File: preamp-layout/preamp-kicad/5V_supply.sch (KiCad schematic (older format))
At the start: 20 parts, among them J12 Conn_01x02_Male, J13 Conn_01x02_Male, J14 Conn_01x02_Male, J15 Screw_Terminal_01x03, T2 Transformer_1P_2S, U3 L7805

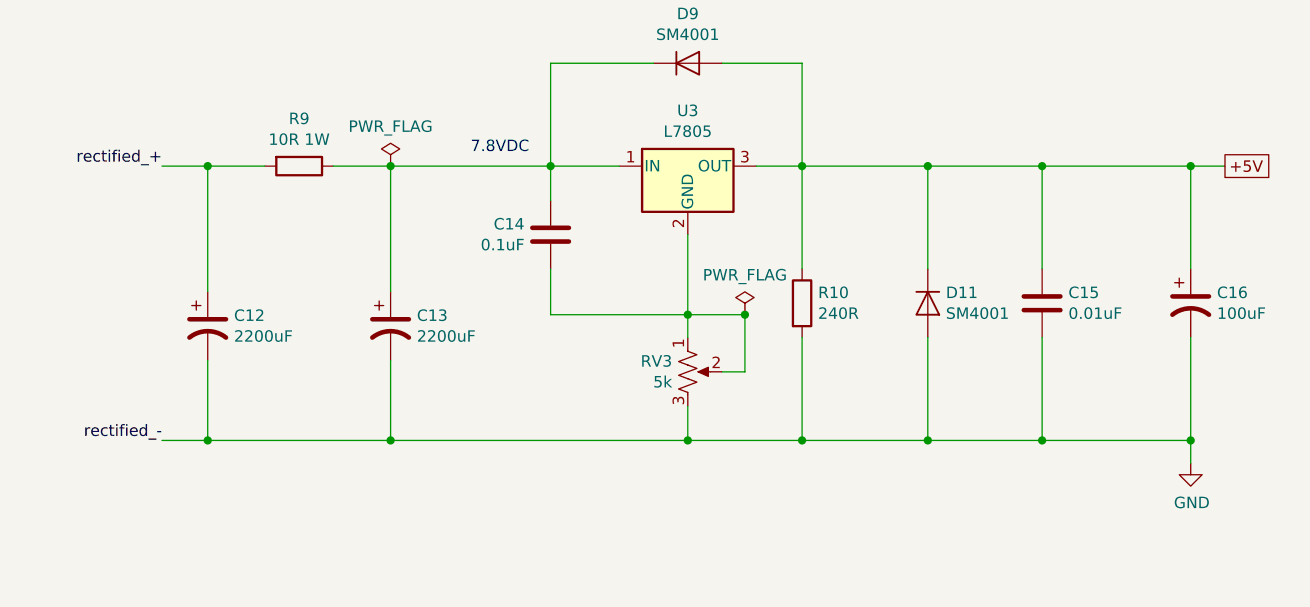
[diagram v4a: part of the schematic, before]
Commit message: Footprint assignment updates
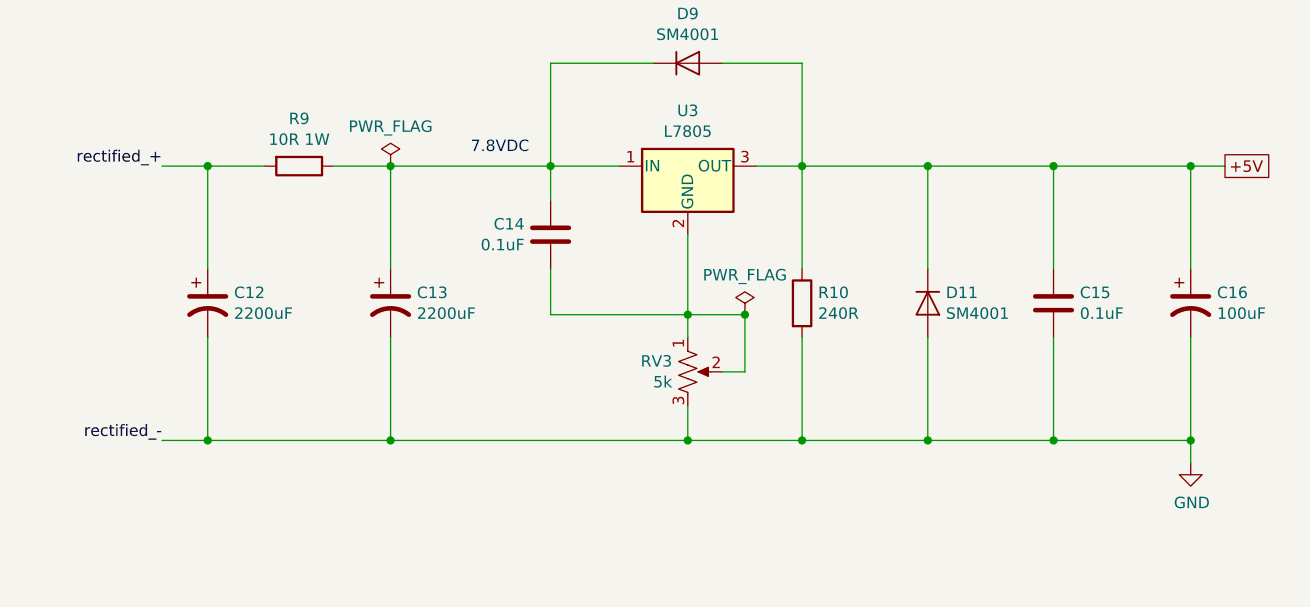
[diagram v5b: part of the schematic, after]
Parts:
- C12, C13: footprint (none) -> Capacitor_THT:CP_Radial_D12.5mm_P5.00mm
- C14: footprint (none) -> Capacitor_SMD:C_0805_2012Metric_Pad1.15x1.40mm_HandSolder
- C15: value 0.01uF -> 0.1uF; footprint (none) -> Capacitor_SMD:C_0805_2012Metric_Pad1.15x1.40mm_HandSolder
- C16: footprint (none) -> Capacitor_THT:CP_Radial_D6.3mm_P2.50mm
- R10: footprint (none) -> Resistor_SMD:R_1206_3216Metric_Pad1.42x1.75mm_HandSolder
- R9: footprint (none) -> Resistor_THT:R_Axial_DIN0414_L11.9mm_D4.5mm_P15.24mm_Horizontal
- U3: footprint (none) -> Package_TO_SOT_THT:TO-220-3_Vertical
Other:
- moved on the sheet: C12, C13, C15
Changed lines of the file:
@@
 L Device:C C?
 U 1 1 5FCCFC4E
-P 7500 4400
+P 7550 4400
 AR Path="/5FCCFC4E" Ref="C?"  Part="1"
 AR Path="/5E27B612/5FCCFC4E" Ref="C?"  Part="1"
 AR Path="/5E5EF2D4/5FCCFC4E" Ref="C15"  Part="1"
-F 0 "C15" H 7615 4446 50  0000 L CNN
-F 1 "0.01uF" H 7615 4355 50  0000 L CNN
-F 2 "" H 7538 4250 50  0001 C CNN
-F 3 "~" H 7500 4400 50  0001 C CNN
-	1    7500 4400
+F 0 "C15" H 7665 4446 50  0000 L CNN
+F 1 "0.1uF" H 7665 4355 50  0000 L CNN
+F 2 "Capacitor_SMD:C_0805_2012Metric_Pad1.15x1.40mm_HandSolder" H 7588 4250 50  0001 C CNN
+F 3 "~" H 7550 4400 50  0001 C CNN
+	1    7550 4400
 	1    0    0    -1
 $EndComp
@@
 F 0 "R10" H 6520 4446 50  0000 L CNN
 F 1 "240R" H 6520 4355 50  0000 L CNN
-F 2 "" V 6380 4400 50  0001 C CNN
+F 2 "Resistor_SMD:R_1206_3216Metric_Pad1.42x1.75mm_HandSolder" V 6380 4400 50  0001 C CNN
 F 3 "~" H 6450 4400 50  0001 C CNN
 	1    6450 4400
@@
 F 0 "R9" V 4043 3800 50  0000 C CNN
 F 1 "10R 1W" V 4134 3800 50  0000 C CNN
-F 2 "" V 4180 3800 50  0001 C CNN
+F 2 "Resistor_THT:R_Axial_DIN0414_L11.9mm_D4.5mm_P15.24mm_Horizontal" V 4180 3800 50  0001 C CNN
 F 3 "~" H 4250 3800 50  0001 C CNN
 	1    4250 3800
@@
 Connection ~ 5350 3800
 Wire Wire Line
-	3850 3800 4100 3800
-Wire Wire Line
 	5950 4850 5950 5000
-Connection ~ 4650 5000
 Connection ~ 5950 5000
 $Comp
@@
 F 0 "C14" H 5236 4146 50  0000 R CNN
 F 1 "0.1uF" H 5236 4055 50  0000 R CNN
-F 2 "" H 5388 3950 50  0001 C CNN
+F 2 "Capacitor_SMD:C_0805_2012Metric_Pad1.15x1.40mm_HandSolder" H 5388 3950 50  0001 C CNN
 F 3 "~" H 5350 4100 50  0001 C CNN
 	1    5350 4100
 	1    0    0    -1
 $EndComp
-$Comp
-L Device:CP1 C?
-U 1 1 5FCCFCBE
-P 3850 4500
-AR Path="/5FCCFCBE" Ref="C?"  Part="1"
-AR Path="/5E27B612/5FCCFCBE" Ref="C?"  Part="1"
-AR Path="/5E5EF2D4/5FCCFCBE" Ref="C12"  Part="1"
-F 0 "C12" H 3965 4546 50  0000 L CNN
-F 1 "2200uF" H 3965 4455 50  0000 L CNN
-F 2 "" H 3850 4500 50  0001 C CNN
-F 3 "~" H 3850 4500 50  0001 C CNN
-	1    3850 4500
-	1    0    0    -1
-$EndComp
-$Comp
-L Device:CP1 C?
-U 1 1 5FCCFCC4
-P 4650 4500
-AR Path="/5FCCFCC4" Ref="C?"  Part="1"
-AR Path="/5E27B612/5FCCFCC4" Ref="C?"  Part="1"
-AR Path="/5E5EF2D4/5FCCFCC4" Ref="C13"  Part="1"
-F 0 "C13" H 4765 4546 50  0000 L CNN
-F 1 "2200uF" H 4765 4455 50  0000 L CNN
-F 2 "" H 4650 4500 50  0001 C CNN
-F 3 "~" H 4650 4500 50  0001 C CNN
-	1    4650 4500
-	1    0    0    -1
-$EndComp
 Wire Wire Line
 	6100 3350 6450 3350
@@
 Wire Wire Line
 	5350 3350 5350 3800
-Wire Wire Line
-	3850 5000 4650 5000
-Wire Wire Line
-	3850 4350 3850 3800
-Wire Wire Line
-	4650 4350 4650 3800
-Wire Wire Line
-	3850 4650 3850 5000
-Wire Wire Line
-	4650 4650 4650 5000
 Wire Wire Line
 	4650 3800 5350 3800
 Connection ~ 4650 3800
 Wire Wire Line
-	7500 4250 7500 3800
-Connection ~ 7500 3800
+	7550 4250 7550 3800
 Wire Wire Line
 	8150 4250 8150 3800
@@
 F 0 "C16" H 8265 4446 50  0000 L CNN
 F 1 "100uF" H 8265 4355 50  0000 L CNN
-F 2 "" H 8150 4400 50  0001 C CNN
+F 2 "Capacitor_THT:CP_Radial_D6.3mm_P2.50mm" H 8150 4400 50  0001 C CNN
 F 3 "~" H 8150 4400 50  0001 C CNN
 	1    8150 4400
@@
 F 0 "U3" H 5950 4042 50  0000 C CNN
 F 1 "L7805" H 5950 3951 50  0000 C CNN
-F 2 "" H 5975 3650 50  0001 L CIN
+F 2 "Package_TO_SOT_THT:TO-220-3_Vertical" H 5975 3650 50  0001 L CIN
 F 3 "http://www.st.com/content/ccc/resource/technical/document/datasheet/41/4f/b3/b0/12/d4/47/88/CD00000444.pdf/files/CD00000444.pdf/jcr:content/translations/en.CD00000444.pdf" H 5950 3750 50  0001 C CNN
 	1    5950 3800
@@
 	6200 4450 5950 4450
 Wire Wire Line
-	4650 5000 5950 5000
-Wire Wire Line
 	5350 3800 5350 3950
 Wire Wire Line
@@
 Connection ~ 7000 5000
 Wire Wire Line
-	7000 5000 7500 5000
-Wire Wire Line
-	7500 4550 7500 5000
-Connection ~ 7500 5000
-Wire Wire Line
-	7500 5000 8150 5000
-Wire Wire Line
-	7500 3800 8150 3800
-Wire Wire Line
-	7000 3800 7500 3800
+	7550 4550 7550 5000
 Wire Wire Line
 	8150 5100 8150 5000
 Connection ~ 8150 5000
-Wire Wire Line
-	3850 3800 3650 3800
-Connection ~ 3850 3800
-Wire Wire Line
-	3850 5000 3650 5000
-Connection ~ 3850 5000
 Wire Wire Line
 	1550 5850 1550 5950
@@
 Wire Wire Line
 	4400 1500 4400 1700
+$Comp
+L Device:CP1 C?
+U 1 1 5FCCFCC4
+P 4650 4400
+AR Path="/5FCCFCC4" Ref="C?"  Part="1"
+AR Path="/5E27B612/5FCCFCC4" Ref="C?"  Part="1"
+AR Path="/5E5EF2D4/5FCCFCC4" Ref="C13"  Part="1"
+F 0 "C13" H 4765 4446 50  0000 L CNN
+F 1 "2200uF" H 4765 4355 50  0000 L CNN
+F 2 "Capacitor_THT:CP_Radial_D12.5mm_P5.00mm" H 4650 4400 50  0001 C CNN
+F 3 "~" H 4650 4400 50  0001 C CNN
+	1    4650 4400
+	1    0    0    -1
+$EndComp
+$Comp
+L Device:CP1 C?
+U 1 1 5FCCFCBE
+P 3850 4400
+AR Path="/5FCCFCBE" Ref="C?"  Part="1"
+AR Path="/5E27B612/5FCCFCBE" Ref="C?"  Part="1"
+AR Path="/5E5EF2D4/5FCCFCBE" Ref="C12"  Part="1"
+F 0 "C12" H 3965 4446 50  0000 L CNN
+F 1 "2200uF" H 3965 4355 50  0000 L CNN
+F 2 "Capacitor_THT:CP_Radial_D12.5mm_P5.00mm" H 3850 4400 50  0001 C CNN
+F 3 "~" H 3850 4400 50  0001 C CNN
+	1    3850 4400
+	1    0    0    -1
+$EndComp
+Wire Wire Line
+	3650 3800 3850 3800
+Wire Wire Line
+	3650 5000 3850 5000
+Wire Wire Line
+	3850 4250 3850 3800
+Connection ~ 3850 3800
+Wire Wire Line
+	3850 3800 4100 3800
+Wire Wire Line
+	4650 4250 4650 3800
+Wire Wire Line
+	3850 4550 3850 5000
+Connection ~ 3850 5000
+Wire Wire Line
+	3850 5000 4650 5000
+Wire Wire Line
+	4650 4550 4650 5000
+Connection ~ 4650 5000
+Wire Wire Line
+	4650 5000 5950 5000
+Connection ~ 7550 3800
+Wire Wire Line
+	7550 3800 8150 3800
+Connection ~ 7550 5000
+Wire Wire Line
+	7550 5000 8150 5000
+Wire Wire Line
+	7000 5000 7550 5000
+Wire Wire Line
+	7000 3800 7550 3800
 $EndSCHEMATC

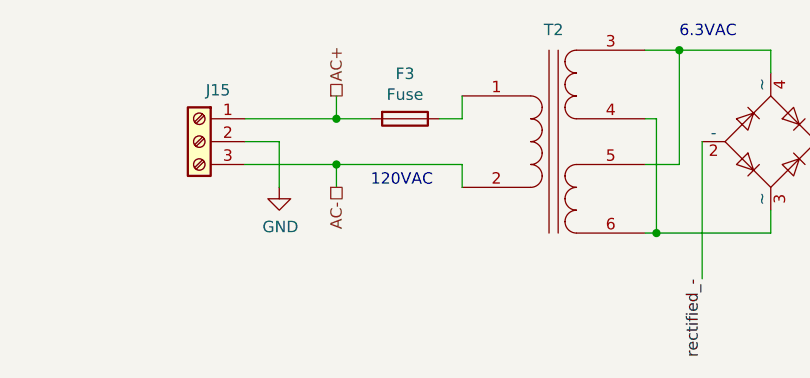
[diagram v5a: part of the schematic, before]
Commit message: Footprint updates
Footprint creation of relay, ESP32
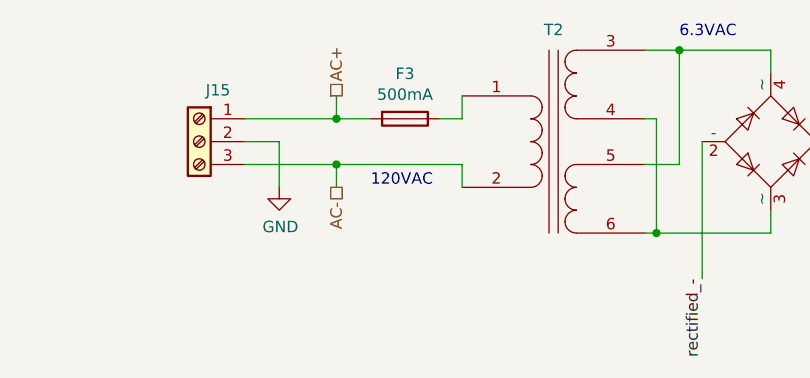
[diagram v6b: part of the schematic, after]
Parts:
- D11, D9: footprint (none) -> Diode_SMD:D_SOD-123F
- F3: value Fuse -> 500mA
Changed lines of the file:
@@
 F 0 "D9" H 5950 3566 50  0000 C CNN
 F 1 "SM4001" H 5950 3475 50  0000 C CNN
-F 2 "" H 5950 3350 50  0001 C CNN
+F 2 "Diode_SMD:D_SOD-123F" H 5950 3350 50  0001 C CNN
 F 3 "~" H 5950 3350 50  0001 C CNN
 	1    5950 3350
@@
 AR Path="/5E5EF2D4/5FD91D98" Ref="F3"  Part="1"
 F 0 "F3" V 4753 1400 50  0000 C CNN
-F 1 "Fuse" V 4844 1400 50  0000 C CNN
+F 1 "500mA" V 4844 1400 50  0000 C CNN
 F 2 "" V 4880 1400 50  0001 C CNN
 F 3 "~" H 4950 1400 50  0001 C CNN
@@
 F 0 "D11" V 6954 4479 50  0000 L CNN
 F 1 "SM4001" V 7045 4479 50  0000 L CNN
-F 2 "" H 7000 4400 50  0001 C CNN
+F 2 "Diode_SMD:D_SOD-123F" H 7000 4400 50  0001 C CNN
 F 3 "~" H 7000 4400 50  0001 C CNN
 	1    7000 4400

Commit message: balanced IO update
other general minor updates
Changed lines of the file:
@@
 Connection ~ 8150 3800
 Wire Wire Line
-	8150 3800 8300 3800
+	8150 3800 8150 3650
 $Comp
 L Device:CP1 C?
@@
 Text GLabel 3000 6050 1    50   UnSpc ~ 0
 +5V
-Text GLabel 8300 3800 2    50   UnSpc ~ 0
-+5V
-$Comp
+Text GLabel 8150 3650 1    50   UnSpc ~ 0
++5V
+$Comp

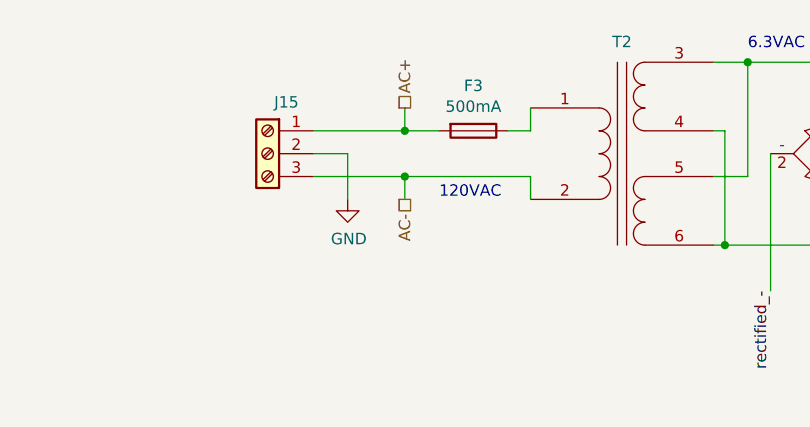
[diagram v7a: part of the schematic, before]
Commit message: Power Supply Update
Grounding made more clear, tied to chassis on AC board. Pins renamed. Aligned with AC wall power convention. General cleanup.
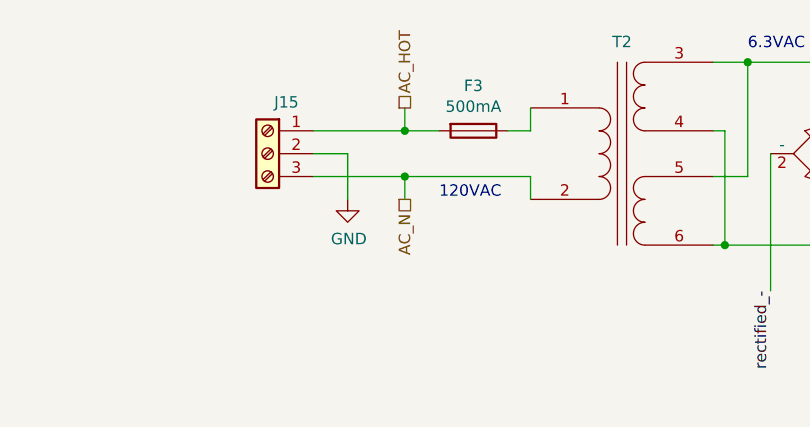
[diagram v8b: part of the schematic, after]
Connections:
- net AC+ renamed AC_HOT
- net AC- renamed AC_N
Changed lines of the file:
@@
 Connection ~ 6200 4450
 Text HLabel 4650 1300 1    50   UnSpc ~ 0
-AC+
+AC_HOT
 Text HLabel 4650 1700 3    50   UnSpc ~ 0
-AC-
+AC_N
 Text Label 6250 2100 3    50   ~ 0
 rectified_-
